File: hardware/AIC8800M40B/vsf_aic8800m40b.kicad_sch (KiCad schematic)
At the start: 86 parts, among them J1 USB_A, J2 USB_C_Receptacle_USB2.0, J3 USB_C_Receptacle_USB2.0, J4 Micro_SD_Card_Det1, J6 Conn_Coaxial, J7 Conn_Coaxial, J8 Conn_01x05, Q1 S9013, SW1 SW_Push, SW2 SW_Push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

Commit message: [hardware/aic8800m40b] update
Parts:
- C16: value 2pF -> 1pF
- C17: value 0.5pF -> NC
- C18: value NC -> 0.5pF
- C22: value 1.5pF -> 1.5nH
- R1: value 2nH -> 1.5nH
- R4: value 1.1nH -> 3pF
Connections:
- net GPIOA10: now also J4.1 (DAT2); no longer J4.8 (DAT1)
- net GPIOA11: now also J4.2 (DAT3/CD); no longer J4.7 (DAT0)
- net GPIOA12: now also J4.3 (CMD); no longer J4.5 (CLK)
- net GPIOA13: now also J4.5 (CLK); no longer J4.3 (CMD)
- net GPIOA14: now also J4.7 (DAT0); no longer J4.2 (DAT3/CD)
- net GPIOA15: now also J4.8 (DAT1); no longer J4.1 (DAT2)
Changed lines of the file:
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@@
     (stroke (width 0) (type default))
   )
+  (wire (pts (xy 139.7 144.78) (xy 165.1 144.78))
+    (stroke (width 0) (type default))
+  )
   (wire (pts (xy 36.83 138.43) (xy 30.48 138.43))
     (stroke (width 0) (type default))
@@
     (stroke (width 0) (type default))
   )
-  (wire (pts (xy 139.7515 147.2589) (xy 165.1515 147.2589))
-    (stroke (width 0) (type default))
-  )
   (wire (pts (xy 194.31 80.01) (xy 201.93 80.01))
     (stroke (width 0) (type default))
@@
     (stroke (width 0) (type default))
   )
+  (wire (pts (xy 139.7 149.86) (xy 165.1 149.86))
+    (stroke (width 0) (type default))
+  )
   (wire (pts (xy 92.71 29.21) (xy 99.06 29.21))
     (stroke (width 0) (type default))
@@
     (stroke (width 0) (type default))
   )
-  (wire (pts (xy 139.7515 149.7989) (xy 165.1515 149.7989))
+  (wire (pts (xy 139.7 147.32) (xy 165.1 147.32))
     (stroke (width 0) (type default))
   )
@@
     (stroke (width 0) (type default))
   )
-  (wire (pts (xy 139.7515 144.7189) (xy 165.1515 144.7189))
-    (stroke (width 0) (type default))
-  )
   (wire (pts (xy 85.09 168.91) (xy 85.09 181.61))
     (stroke (width 0) (type default))
@@
     (stroke (width 0) (type default))
   )
-  (wire (pts (xy 139.7515 154.8789) (xy 165.1515 154.8789))
-    (stroke (width 0) (type default))
-  )
   (wire (pts (xy 238.76 134.62) (xy 243.84 134.62))
     (stroke (width 0) (type default))
@@
     (stroke (width 0) (type default))
   )
-  (wire (pts (xy 139.7515 142.1789) (xy 165.1515 142.1789))
-    (stroke (width 0) (type default))
-  )
   (wire (pts (xy 90.17 168.91) (xy 90.17 176.53))
     (stroke (width 0) (type default))
@@
     (stroke (width 0) (type default))
   )
+  (wire (pts (xy 139.7 142.24) (xy 165.1 142.24))
+    (stroke (width 0) (type default))
+  )
   (wire (pts (xy 241.3 144.78) (xy 241.3 137.16))
     (stroke (width 0) (type default))
@@
     (stroke (width 0) (type default))
   )
+  (wire (pts (xy 139.7 152.4) (xy 165.1 152.4))
+    (stroke (width 0) (type default))
+  )
   (wire (pts (xy 59.69 168.91) (xy 59.69 181.61))
     (stroke (width 0) (type default))
@@
     (stroke (width 0) (type default))
   )
+  (wire (pts (xy 139.7 154.94) (xy 165.1 154.94))
+    (stroke (width 0) (type default))
+  )
   (wire (pts (xy 62.23 91.44) (xy 67.31 91.44))
     (stroke (width 0) (type default))
@@
     (stroke (width 0) (type default))
   )
-  (wire (pts (xy 139.7515 152.3389) (xy 165.1515 152.3389))
-    (stroke (width 0) (type default))
-  )
   (wire (pts (xy 140.97 34.29) (xy 146.05 34.29))
     (stroke (width 0) (type default))
@@
     (effects (font (size 1.27 1.27)) (justify right bottom))
   )
-  (label "SDIO_CLK" (at 139.7515 142.1789 0) (fields_autoplaced)
+  (label "SDIO_CLK" (at 139.7 142.24 0) (fields_autoplaced)
     (effects (font (size 1.27 1.27)) (justify left bottom))
   )
@@
     (effects (font (size 1.27 1.27)) (justify left bottom))
   )
-  (label "GPIOA11" (at 165.1515 147.2589 180) (fields_autoplaced)
+  (label "GPIOA11" (at 165.1 154.94 180) (fields_autoplaced)
     (effects (font (size 1.27 1.27)) (justify right bottom))
   )
@@
     (effects (font (size 1.27 1.27)) (justify right bottom))
   )
-  (label "GPIOA15" (at 165.1515 152.3389 180) (fields_autoplaced)
+  (label "GPIOA15" (at 165.1 149.86 180) (fields_autoplaced)
     (effects (font (size 1.27 1.27)) (justify right bottom))
   )
@@
     (effects (font (size 1.27 1.27)) (justify left bottom))
   )
-  (label "SDIO_DAT1" (at 139.7515 149.7989 0) (fields_autoplaced)
+  (label "SDIO_DAT1" (at 139.7 149.86 0) (fields_autoplaced)
     (effects (font (size 1.27 1.27)) (justify left bottom))
   )
@@
     (effects (font (size 1.27 1.27)) (justify left bottom))
   )
-  (label "SDIO_DAT2" (at 139.7515 152.3389 0) (fields_autoplaced)
+  (label "SDIO_DAT2" (at 139.7 152.4 0) (fields_autoplaced)
     (effects (font (size 1.27 1.27)) (justify left bottom))
   )
@@
     (effects (font (size 1.27 1.27)) (justify left bottom))
   )
-  (label "SDIO_CMD" (at 139.7515 144.7189 0) (fields_autoplaced)
+  (label "SDIO_CMD" (at 139.7 144.78 0) (fields_autoplaced)
     (effects (font (size 1.27 1.27)) (justify left bottom))
   )
@@
     (effects (font (size 1.27 1.27)) (justify left bottom))
   )
-  (label "GPIOA10" (at 165.1515 149.7989 180) (fields_autoplaced)
+  (label "GPIOA10" (at 165.1 152.4 180) (fields_autoplaced)
     (effects (font (size 1.27 1.27)) (justify right bottom))
   )
@@
     (effects (font (size 1.27 1.27)) (justify right bottom))
   )
-  (label "GPIOA12" (at 165.1515 142.1789 180) (fields_autoplaced)
+  (label "GPIOA12" (at 165.1 144.78 180) (fields_autoplaced)
     (effects (font (size 1.27 1.27)) (justify right bottom))
   )
@@
     (effects (font (size 1.27 1.27)) (justify left bottom))
   )
-  (label "SDIO_DAT0" (at 139.7515 147.2589 0) (fields_autoplaced)
+  (label "SDIO_DAT0" (at 139.7 147.32 0) (fields_autoplaced)
     (effects (font (size 1.27 1.27)) (justify left bottom))
   )
@@
     (effects (font (size 1.27 1.27)) (justify right bottom))
   )
-  (label "GPIOA13" (at 165.1515 144.7189 180) (fields_autoplaced)
+  (label "GPIOA13" (at 165.1 142.24 180) (fields_autoplaced)
     (effects (font (size 1.27 1.27)) (justify right bottom))
   )
@@
     (effects (font (size 1.27 1.27)) (justify left bottom))
   )
-  (label "GPIOA14" (at 165.1515 154.8789 180) (fields_autoplaced)
+  (label "GPIOA14" (at 165.1 147.32 180) (fields_autoplaced)
     (effects (font (size 1.27 1.27)) (justify right bottom))
   )
@@
     (effects (font (size 1.27 1.27)) (justify right bottom))
   )
-  (label "SDIO_DAT3" (at 139.7515 154.8789 0) (fields_autoplaced)
+  (label "SDIO_DAT3" (at 139.7 154.94 0) (fields_autoplaced)
     (effects (font (size 1.27 1.27)) (justify left bottom))
   )
@@
       (effects (font (size 1.27 1.27)) (justify left))
     )
-    (property "Value" "1.5pF" (at 97.79 81.28 90)
+    (property "Value" "1.5nH" (at 97.79 81.28 90)
       (effects (font (size 1.27 1.27)) (justify left))
     )
@@
       (effects (font (size 1.27 1.27)))
     )
-    (property "Value" "1.1nH" (at 95.25 86.36 90)
+    (property "Value" "3pF" (at 95.25 86.36 90)
       (effects (font (size 1.27 1.27)))
     )
@@
       (effects (font (size 1.27 1.27)) (justify left))
     )
-    (property "Value" "NC" (at 52.07 80.01 0)
+    (property "Value" "0.5pF" (at 52.07 80.01 0)
       (effects (font (size 1.27 1.27)) (justify left))
     )
@@
       (effects (font (size 1.27 1.27)) (justify left))
     )
-    (property "Value" "2pF" (at 52.07 97.79 0)
+    (property "Value" "1pF" (at 52.07 97.79 0)
       (effects (font (size 1.27 1.27)) (justify left))
     )
@@
       (effects (font (size 1.27 1.27)))
     )
-    (property "Value" "2nH" (at 57.15 91.44 90)
+    (property "Value" "1.5nH" (at 57.15 91.44 90)
       (effects (font (size 1.27 1.27)))
     )
@@
       (effects (font (size 1.27 1.27)) (justify left))
     )
-    (property "Value" "0.5pF" (at 59.69 81.28 90)
+    (property "Value" "NC" (at 59.69 81.28 90)
       (effects (font (size 1.27 1.27)) (justify left))
     )

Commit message: [hardware/aic8800m40b] update
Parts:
- L4: footprint Inductor_SMD:L_2010_5025Metric -> Inductor_SMD:L_1210_3225Metric
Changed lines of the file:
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@@
       (effects (font (size 1.27 1.27)))
     )
-    (property "Footprint" "Inductor_SMD:L_2010_5025Metric" (at 246.38 69.85 0)
+    (property "Footprint" "Inductor_SMD:L_1210_3225Metric" (at 246.38 69.85 0)
       (effects (font (size 1.27 1.27)) hide)
     )
@@
       (effects (font (size 1.27 1.27)))
     )
-    (property "Footprint" "Inductor_SMD:L_2010_5025Metric" (at 223.52 36.83 0)
-      (effects (font (size 1.27 1.27)) hide)
-    )
+    (property "Footprint" "Inductor_SMD:L_1210_3225Metric" (at 223.52 36.83 0)
+      (effects (font (size 1.27 1.27)) hide)
+    )

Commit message: [hardware/aic8800m40b] update footprint of L1 to be 0805
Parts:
- L1: footprint Inductor_SMD:L_0603_1608Metric -> Inductor_SMD:L_0805_2012Metric
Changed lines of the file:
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@@
       (effects (font (size 1.27 1.27)))
     )
-    (property "Footprint" "Inductor_SMD:L_0603_1608Metric" (at 107.95 153.67 0)
+    (property "Footprint" "Inductor_SMD:L_0805_2012Metric" (at 107.95 153.67 0)
       (effects (font (size 1.27 1.27)) hide)
     )

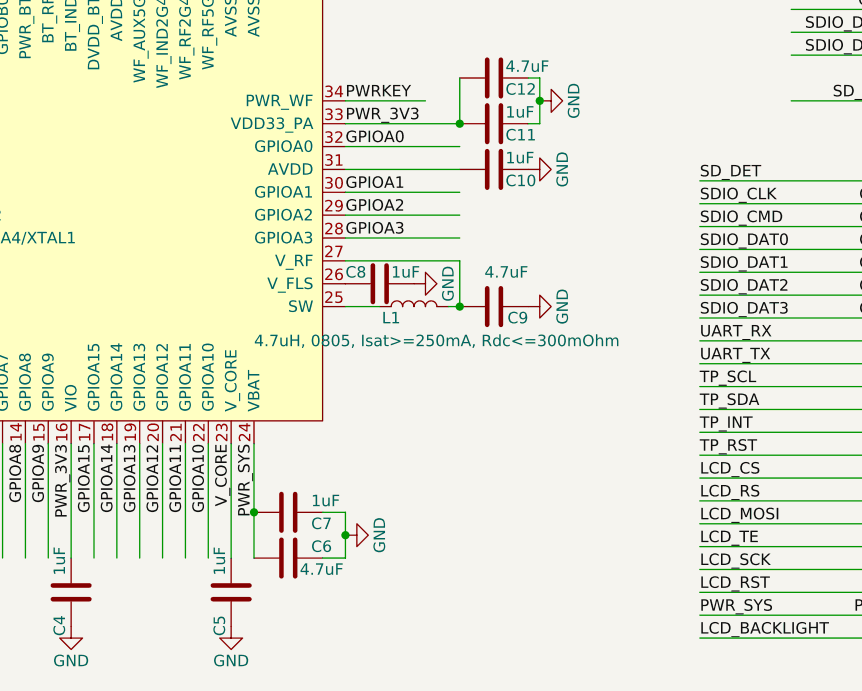
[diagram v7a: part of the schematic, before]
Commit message: [hardware/aic8800m40b] add test points
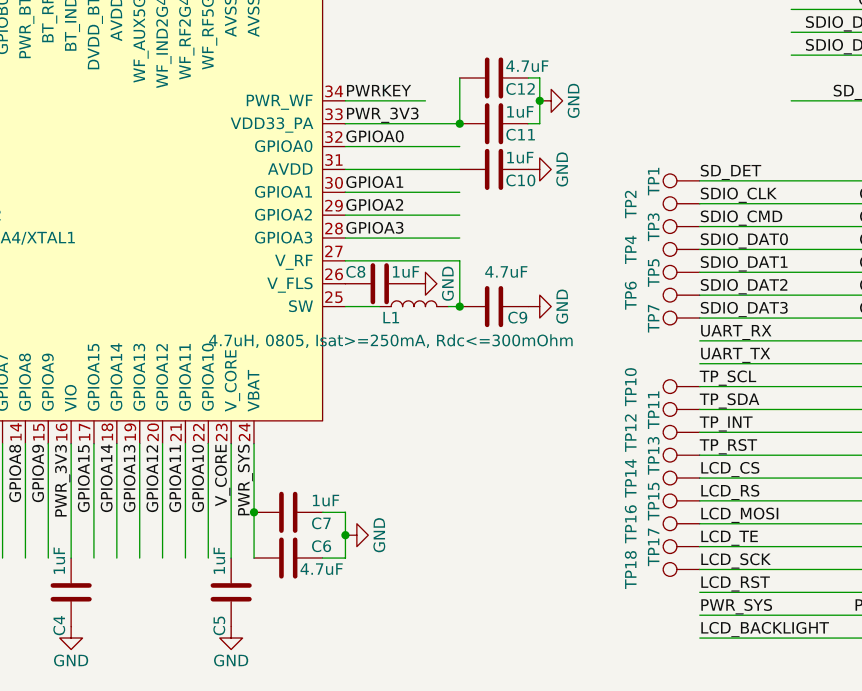
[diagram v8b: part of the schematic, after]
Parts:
- added TP1, TP10, TP11, TP12, TP13, TP14, TP15, TP16, TP17, TP18, TP2, TP3, TP4, TP5, TP6, TP7: TestPoint, TestPoint:TestPoint_Pad_D1.0mm, symbol Connector:TestPoint
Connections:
- net GPIOA0: now also TP18.1
- net GPIOA1: now also TP14.1
- net GPIOA10: now also TP6.1
- net GPIOA11: now also TP7.1
- net GPIOA12: now also TP3.1
- net GPIOA13: now also TP2.1
- net GPIOA14: now also TP4.1
- net GPIOA15: now also TP5.1
- net GPIOA2: now also TP13.1
- net GPIOA3: now also TP16.1
- net GPIOA4: now also TP15.1
- net GPIOA5: now also TP17.1
- net GPIOA6: now also TP10.1
- net GPIOA7: now also TP11.1
- net GPIOB2: now also TP1.1
- net GPIOB3: now also TP12.1
